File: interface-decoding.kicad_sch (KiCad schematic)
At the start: 4 parts

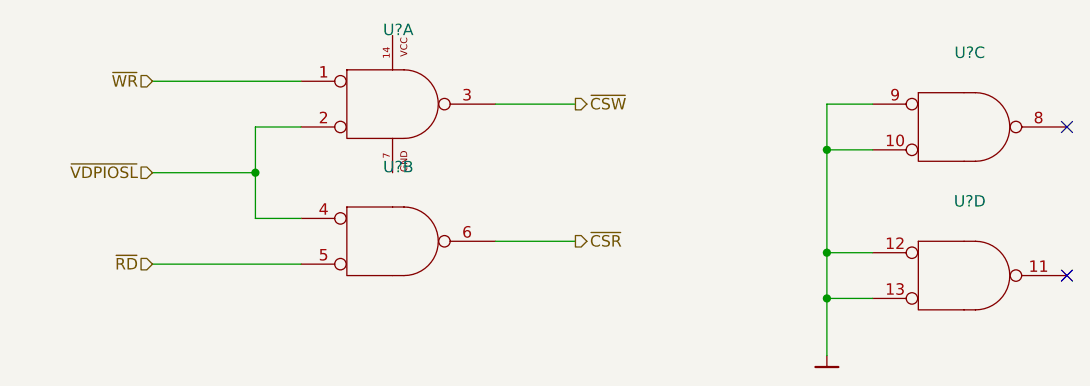
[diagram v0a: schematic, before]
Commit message: Migrate to KiCad v8
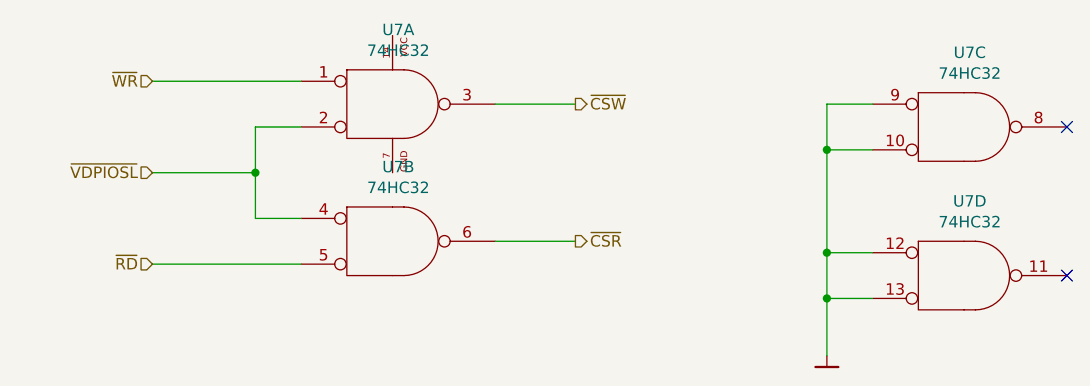
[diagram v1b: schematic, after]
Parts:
- U7: renamed from U?; value (none) -> 74HC32; footprint (none) -> artemisa:DIP-14_300
